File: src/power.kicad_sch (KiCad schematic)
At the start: 28 parts, among them U1 ECP5U_12_CABGA256, U12 TLV62569DRL, U13 TLV62569DRL, U14 TLV62569DRL

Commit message: Rev 2
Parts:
- C10, C27, C29: LCSC Part (none) -> C14858
- C11, C12, C2, C28, C3, C4, C8, C9: LCSC Part (none) -> C19702
- C36, C37, C38, C42: LCSC Part (none) -> C1525
- RA1, RA2, RA3: LCSC Part (none) -> C22809
- RB1: LCSC Part (none) -> C25810
- RB2: LCSC Part (none) -> C23162
- RB3: LCSC Part (none) -> C22978
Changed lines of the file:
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@@
 			)
 		)
+		(property "LCSC Part" "C19702"
+			(at 72.39 72.39 0)
+			(effects
+				(font
+					(size 1.27 1.27)
+				)
+			)
+		)
 		(pin "1"
 		)
@@
 			)
 		)
+		(property "LCSC Part" "C22809"
+			(at 114.3 62.23 0)
+			(effects
+				(font
+					(size 1.27 1.27)
+				)
+			)
+		)
 		(pin "1"
 		)
@@
 			)
 		)
+		(property "LCSC Part" "C25810"
+			(at 119.38 67.31 0)
+			(effects
+				(font
+					(size 1.27 1.27)
+				)
+			)
+		)
 		(pin "1"
 		)
@@
 			)
 		)
-		(property "LCSC Part" ""
+		(property "LCSC Part" "C19702"
 			(at 106.68 123.19 0)
 			(effects
@@
 			)
 		)
+		(property "LCSC Part" "C22809"
+			(at 114.3 123.19 0)
+			(effects
+				(font
+					(size 1.27 1.27)
+				)
+			)
+		)
 		(pin "1"
 		)
@@
 			)
 		)
+		(property "LCSC Part" "C22978"
+			(at 119.38 128.27 0)
+			(effects
+				(font
+					(size 1.27 1.27)
+				)
+			)
+		)
 		(pin "1"
 		)
@@
 			)
 		)
-		(property "LCSC Part" ""
+		(property "LCSC Part" "C14858"
 			(at 124.46 123.19 0)
 			(effects
@@
 			)
 		)
+		(property "LCSC Part" "C22809"
+			(at 114.3 92.71 0)
+			(effects
+				(font
+					(size 1.27 1.27)
+				)
+			)
+		)
 		(pin "1"
 		)
@@
 			)
 		)
+		(property "LCSC Part" "C23162"
+			(at 119.38 97.79 0)
+			(effects
+				(font
+					(size 1.27 1.27)
+				)
+			)
+		)
 		(pin "1"
 		)
@@
 			)
 		)
-		(property "LCSC Part" ""
+		(property "LCSC Part" "C1525"
 			(at 246.38 74.93 0)
 			(effects
@@
 			)
 		)
-		(property "LCSC Part" ""
+		(property "LCSC Part" "C14858"
 			(at 124.46 92.71 0)
 			(effects
@@
 			)
 		)
+		(property "LCSC Part" "C19702"
+			(at 72.39 133.35 0)
+			(effects
+				(font
+					(size 1.27 1.27)
+				)
+			)
+		)
 		(pin "1"
 		)
@@
 			)
 		)
-		(property "LCSC Part" ""
+		(property "LCSC Part" "C14858"
 			(at 124.46 62.23 0)
 			(effects
@@
 			)
 		)
-		(property "LCSC Part" ""
+		(property "LCSC Part" "C1525"
 			(at 208.28 74.93 0)
 			(effects
@@
 			)
 		)
+		(property "LCSC Part" "C19702"
+			(at 72.39 102.87 0)
+			(effects
+				(font
+					(size 1.27 1.27)
+				)
+			)
+		)
 		(pin "1"
 		)
@@
 			)
 		)
-		(property "LCSC Part" ""
+		(property "LCSC Part" "C1525"
 			(at 233.68 74.93 0)
 			(effects
@@
 			)
 		)
+		(property "LCSC Part" "C19702"
+			(at 196.85 74.93 0)
+			(effects
+				(font
+					(size 1.27 1.27)
+				)
+			)
+		)
 		(pin "2"
 		)
@@
 			)
 		)
-		(property "LCSC Part" ""
+		(property "LCSC Part" "C19702"
 			(at 106.68 92.71 0)
 			(effects
@@
 			)
 		)
-		(property "LCSC Part" ""
+		(property "LCSC Part" "C1525"
 			(at 220.98 74.93 0)
 			(effects
@@
 			)
 		)
+		(property "LCSC Part" "C19702"
+			(at 184.15 74.93 0)
+			(effects
+				(font
+					(size 1.27 1.27)
+				)
+			)
+		)
 		(pin "2"
 		)
@@
 			)
 		)
-		(property "LCSC Part" ""
+		(property "LCSC Part" "C19702"
 			(at 106.68 62.23 0)
 			(effects

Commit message: Tidy project
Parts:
- C10, C27, C29: JLCPCB Part # (none) -> C14858; LCSC Part C14858 -> (none)
- C11, C12, C2, C28, C3, C4, C8, C9: JLCPCB Part # (none) -> C19702; LCSC Part C19702 -> (none)
- C36, C37, C38, C42: JLCPCB Part # (none) -> C1525; LCSC Part C1525 -> (none)
- L1, L2, L3: JLCPCB Part # (none) -> C285758; LCSC Part C285758 -> (none)
- RA1, RA2, RA3: JLCPCB Part # (none) -> C22809; LCSC Part C22809 -> (none)
- RB1: JLCPCB Part # (none) -> C25810; LCSC Part C25810 -> (none)
- RB2: JLCPCB Part # (none) -> C23162; LCSC Part C23162 -> (none)
- RB3: JLCPCB Part # (none) -> C22978; LCSC Part C22978 -> (none)
- U1: JLCPCB Part # (none) -> C1521614; LCSC Part C1521614 -> (none)
- U12, U13, U14: JLCPCB Part # (none) -> C163217; LCSC Part C163217 -> (none)
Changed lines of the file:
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@@
 			)
 		)
-		(property "LCSC Part" "C19702"
+		(property "JLCPCB Part #" "C19702"
 			(at 72.39 72.39 0)
 			(effects
@@
 			)
 		)
-		(property "LCSC Part" "C22809"
+		(property "JLCPCB Part #" "C22809"
 			(at 114.3 62.23 0)
 			(effects
@@
 			)
 		)
-		(property "LCSC Part" "C25810"
+		(property "JLCPCB Part #" "C25810"
 			(at 119.38 67.31 0)
 			(effects
@@
 			)
 		)
-		(property "LCSC Part" "C19702"
+		(property "JLCPCB Part #" "C19702"
 			(at 106.68 123.19 0)
 			(effects
@@
 					(size 1.27 1.27)
 				)
-				(hide yes)
 			)
 		)
@@
 			)
 		)
-		(property "LCSC Part" "C22809"
+		(property "JLCPCB Part #" "C22809"
 			(at 114.3 123.19 0)
 			(effects
@@
 			)
 		)
-		(property "LCSC Part" "C22978"
+		(property "JLCPCB Part #" "C22978"
 			(at 119.38 128.27 0)
 			(effects
@@
 			)
 		)
-		(property "LCSC Part" "C14858"
+		(property "JLCPCB Part #" "C14858"
 			(at 124.46 123.19 0)
 			(effects
@@
 					(size 1.27 1.27)
 				)
-				(hide yes)
 			)
 		)
@@
 			)
 		)
-		(property "LCSC Part" " C285758"
+		(property "JLCPCB Part #" " C285758"
 			(at 101.6 87.63 0)
 			(effects
@@
 					(size 1.27 1.27)
 				)
-				(hide yes)
 			)
 		)
@@
 			)
 		)
-		(property "LCSC Part" "C22809"
+		(property "JLCPCB Part #" "C22809"
 			(at 114.3 92.71 0)
 			(effects
@@
 			)
 		)
-		(property "LCSC Part" "C23162"
+		(property "JLCPCB Part #" "C23162"
 			(at 119.38 97.79 0)
 			(effects
@@
 			)
 		)
-		(property "LCSC Part" " C285758"
+		(property "JLCPCB Part #" " C285758"
 			(at 101.6 57.15 0)
 			(effects
@@
 					(size 1.27 1.27)
 				)
-				(hide yes)
 			)
 		)
@@
 			)
 		)
-		(property "LCSC Part" " C285758"
+		(property "JLCPCB Part #" " C285758"
 			(at 101.6 118.11 0)
 			(effects
@@
 					(size 1.27 1.27)
 				)
-				(hide yes)
 			)
 		)
@@
 			)
 		)
-		(property "LCSC Part" "C1525"
+		(property "JLCPCB Part #" "C1525"
 			(at 246.38 74.93 0)
 			(effects
@@
 					(size 1.27 1.27)
 				)
-				(hide yes)
 			)
 		)
@@
 			)
 		)
-		(property "LCSC Part" "C14858"
+		(property "JLCPCB Part #" "C14858"
 			(at 124.46 92.71 0)
 			(effects
@@
 					(size 1.27 1.27)
 				)
-				(hide yes)
 			)
 		)
@@
 			)
 		)
-		(property "LCSC Part" "C19702"
+		(property "JLCPCB Part #" "C19702"
 			(at 72.39 133.35 0)
 			(effects
@@
 			)
 		)
-		(property "LCSC Part" "C14858"
+		(property "JLCPCB Part #" "C14858"
 			(at 124.46 62.23 0)
 			(effects
@@
 					(size 1.27 1.27)
 				)
-				(hide yes)
 			)
 		)
@@
 			)
 		)
-		(property "LCSC Part" "C1525"
+		(property "JLCPCB Part #" "C1525"
 			(at 208.28 74.93 0)
 			(effects
@@
 					(size 1.27 1.27)
 				)
-				(hide yes)
 			)
 		)
@@
 			)
 		)
-		(property "LCSC Part" "C163217"
+		(property "JLCPCB Part #" "C163217"
 			(at 85.09 67.31 0)
 			(effects
@@
 			)
 		)
-		(property "LCSC Part" "C19702"
+		(property "JLCPCB Part #" "C19702"
 			(at 72.39 102.87 0)
 			(effects
@@
 			)
 		)
-		(property "LCSC Part" "C163217"
+		(property "JLCPCB Part #" "C163217"
 			(at 85.09 97.79 0)
 			(effects
@@
 			)
 		)
-		(property "LCSC Part" " C1521614"
+		(property "JLCPCB Part #" " C1521614"
 			(at 191.77 91.44 0)
 			(effects
@@
 					(size 1.27 1.27)
 				)
-				(hide yes)
 			)
 		)
@@
 			)
 		)
-		(property "LCSC Part" "C1525"
+		(property "JLCPCB Part #" "C1525"
 			(at 233.68 74.93 0)
 			(effects
@@
 					(size 1.27 1.27)
 				)
-				(hide yes)
 			)
 		)
@@
 			)
 		)
-		(property "LCSC Part" "C19702"
+		(property "JLCPCB Part #" "C19702"
 			(at 196.85 74.93 0)
 			(effects
@@
 			)
 		)
-		(property "LCSC Part" "C19702"
+		(property "JLCPCB Part #" "C19702"
 			(at 106.68 92.71 0)
 			(effects
@@
 					(size 1.27 1.27)
 				)
-				(hide yes)
 			)
 		)
@@
 			)
 		)
-		(property "LCSC Part" "C1525"
+		(property "JLCPCB Part #" "C1525"
 			(at 220.98 74.93 0)
 			(effects
@@
 					(size 1.27 1.27)
 				)
-				(hide yes)
 			)
 		)
@@
 			)
 		)
-		(property "LCSC Part" "C163217"
+		(property "JLCPCB Part #" "C163217"
 			(at 85.09 128.27 0)
 			(effects
@@
 			)
 		)
-		(property "LCSC Part" "C19702"
+		(property "JLCPCB Part #" "C19702"
 			(at 184.15 74.93 0)
 			(effects
@@
 			)
 		)
-		(property "LCSC Part" "C19702"
+		(property "JLCPCB Part #" "C19702"
 			(at 106.68 62.23 0)
 			(effects
@@
 					(size 1.27 1.27)
 				)
-				(hide yes)
 			)
 		)

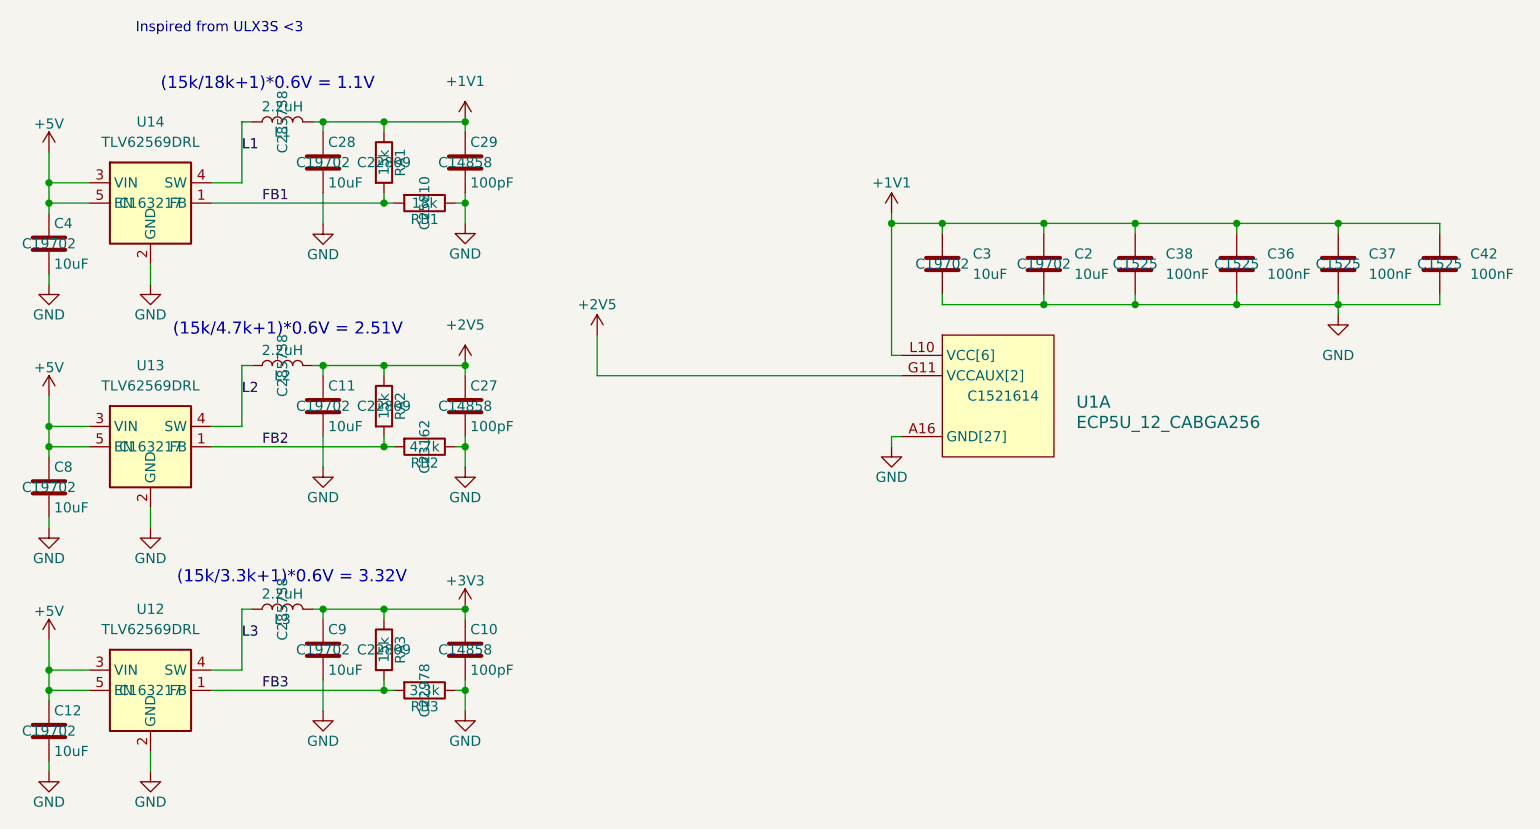
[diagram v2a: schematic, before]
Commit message: Add test points
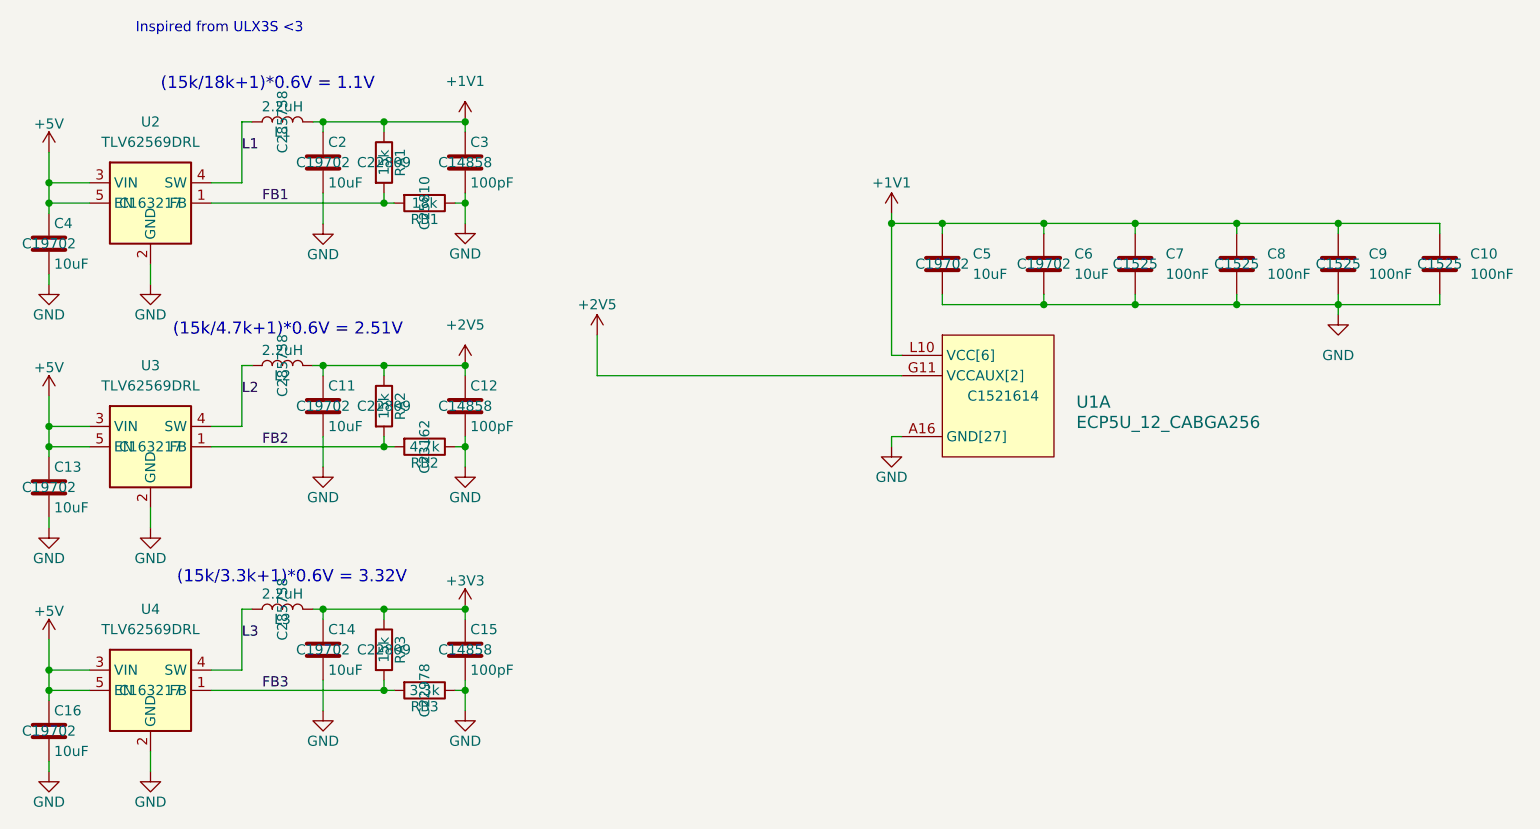
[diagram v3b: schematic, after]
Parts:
- renumbered C42 to C10, C27 to C12, C8 to C13, C9 to C14, C10 to C15, C12 to C16, C28 to C2, C29 to C3, C3 to C5, C2 to C6, C38 to C7, C36 to C8, C37 to C9, U14 to U2, U13 to U3, U12 to U4
